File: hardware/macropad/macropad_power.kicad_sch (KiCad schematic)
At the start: 33 parts, among them J1 Conn_01x04_Pin, J2 USB_C_Receptacle, J3 Conn_02x03_Counter_Clockwise, J4 display(4x1), J5 enc1, J6 enc2, Q1 PMOS, SW1 SW_SPDT, SW10 SW_Push, SW11 SW_Push, SW2 SW_Push, SW3 SW_Push, SW4 SW_Push, SW5 SW_Push, SW6 SW_Push, SW7 SW_Push, SW8 SW_Push, SW9 SW_Push, U1 AP2112K-3.3, U2 STM32F103C8Tx, U3 NRF24L01_Breakout

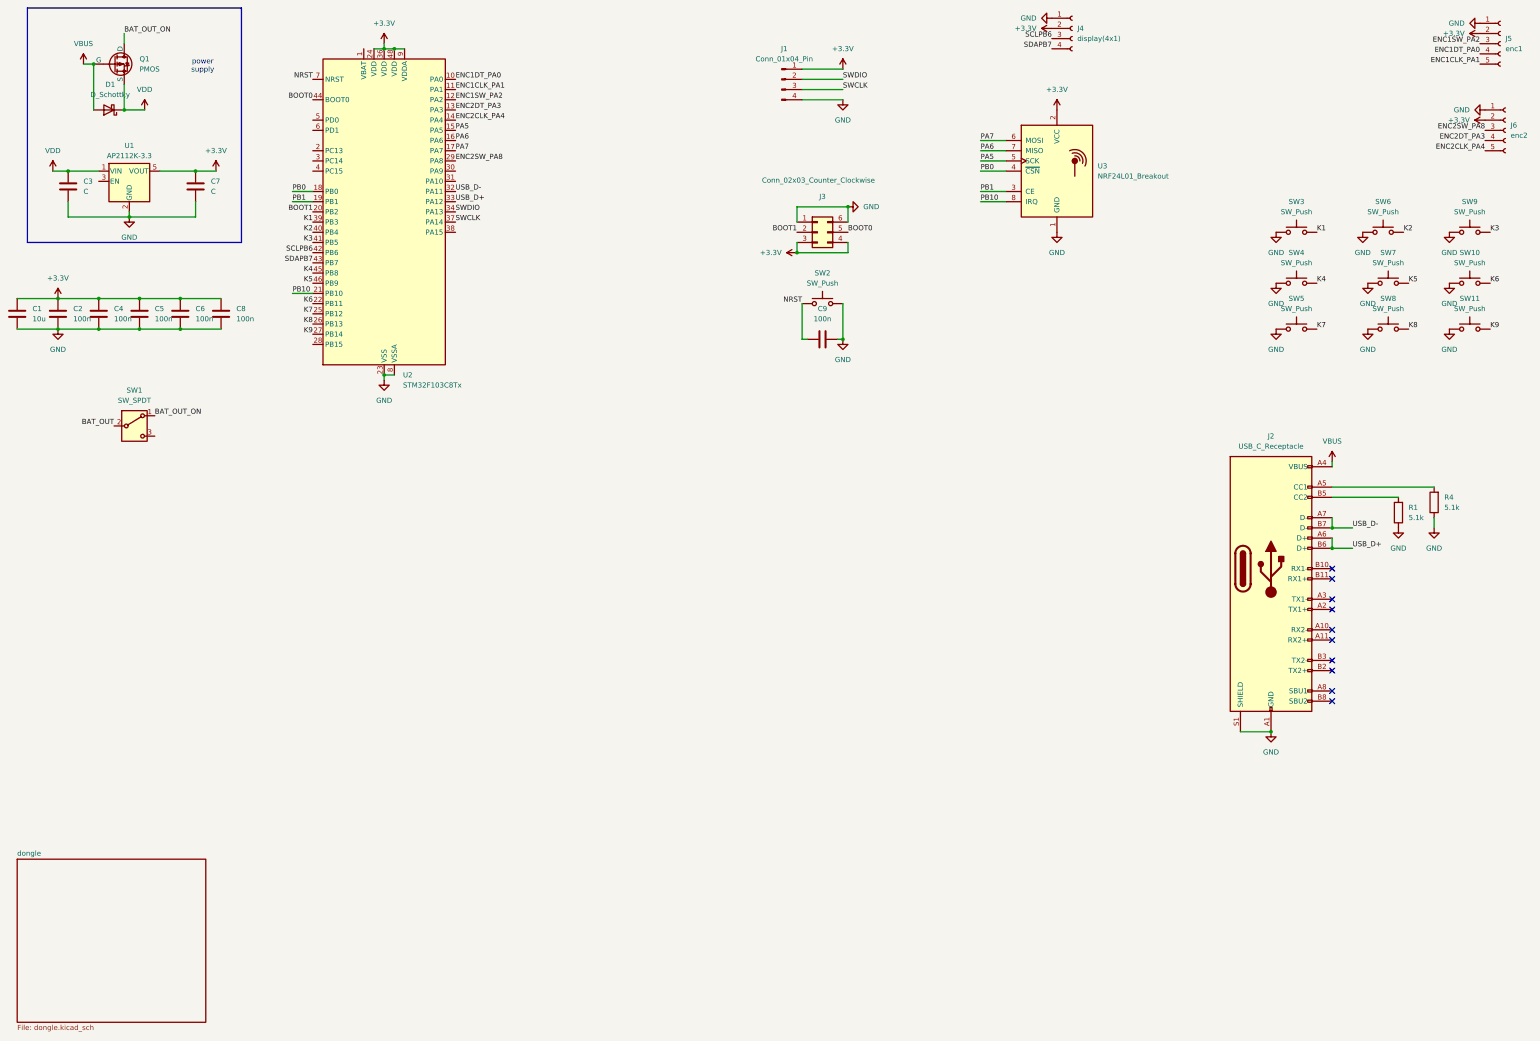
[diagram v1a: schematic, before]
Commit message: captured TP4056 module
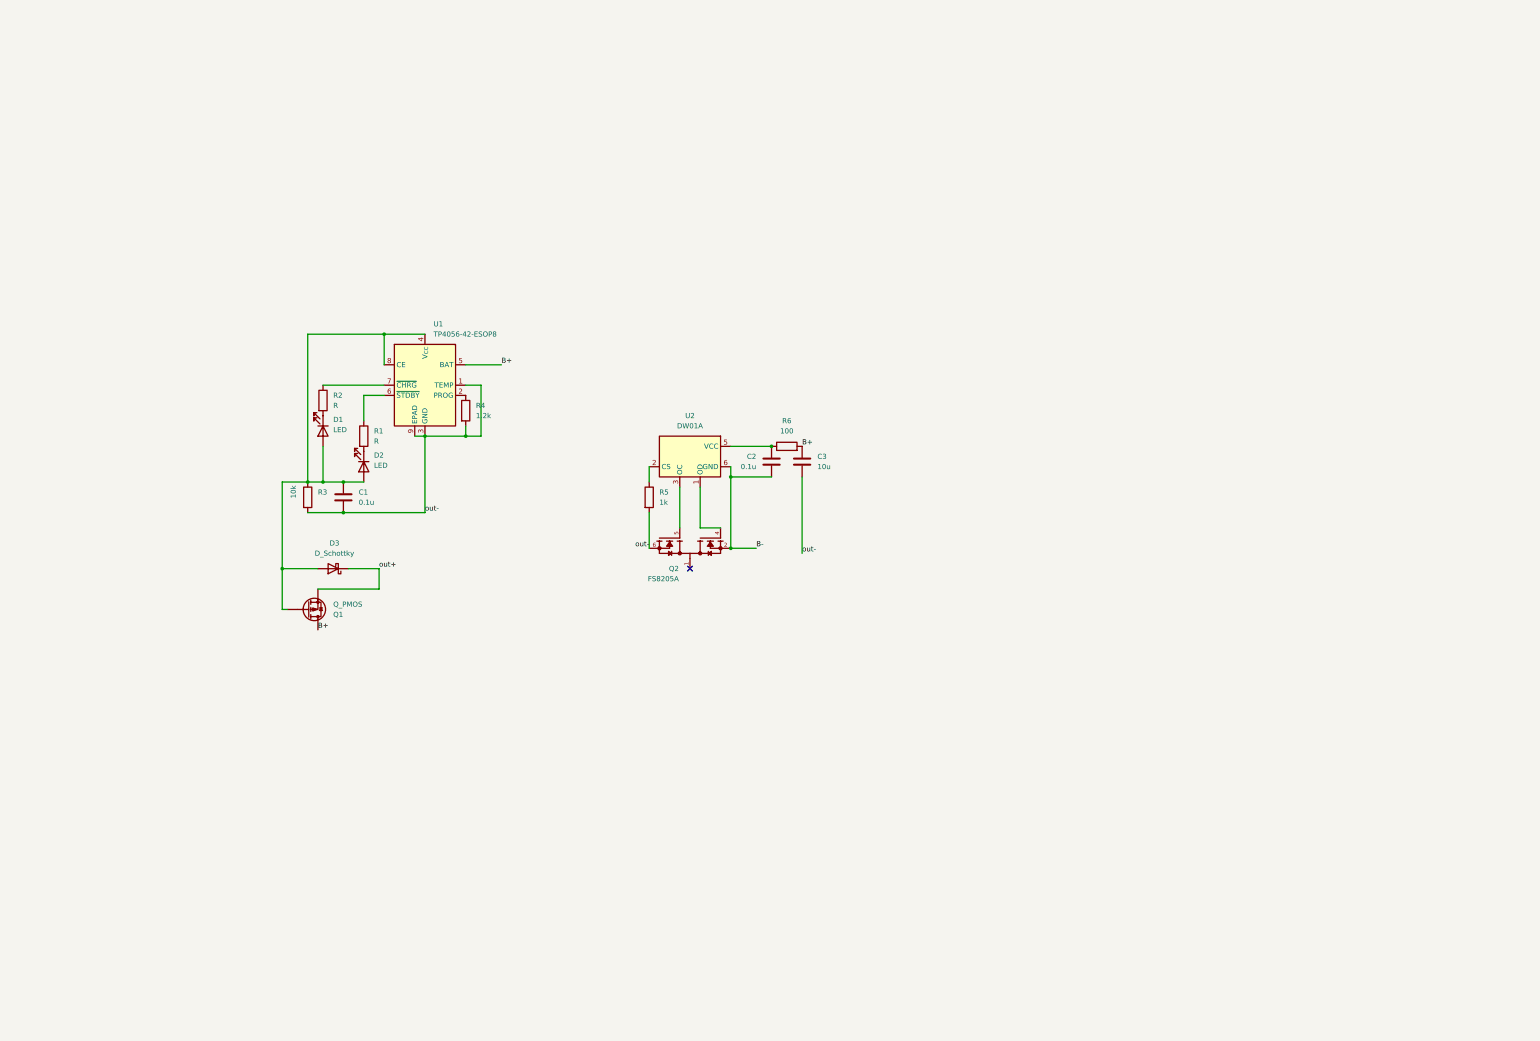
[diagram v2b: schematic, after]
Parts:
- removed C4, C5, C6, C8, C9: 100n, symbol Device:C
- removed C7: C, symbol Device:C
- removed D1: D_Schottky, symbol Device:D_Schottky
- removed J1: Conn_01x04_Pin, Connector_PinHeader_2.54mm:PinHeader_1x04_P2.54mm_Horizontal, symbol Connector:Conn_01x04_Pin
- removed J2: USB_C_Receptacle, symbol Connector:USB_C_Receptacle
- removed J3: Conn_02x03_Counter_Clockwise, symbol Connector_Generic:Conn_02x03_Counter_Clockwise
- removed J4: display(4x1), Connector_PinHeader_2.54mm:PinHeader_1x04_P2.54mm_Vertical, symbol Connector:Conn_01x04_Socket
- removed J5: enc1, Connector_PinHeader_2.54mm:PinHeader_1x05_P2.54mm_Horizontal, symbol Connector:Conn_01x05_Socket
- removed J6: enc2, Connector_PinHeader_2.54mm:PinHeader_1x05_P2.54mm_Horizontal, symbol Connector:Conn_01x05_Socket
- removed Q1: PMOS, symbol Simulation_SPICE:PMOS
- removed SW1: SW_SPDT, symbol Switch:SW_SPDT
- removed SW10, SW11, SW3, SW4, SW5, SW6, SW7, SW8, SW9: SW_Push, keyswitches:Kailh_socket_MX, symbol Switch:SW_Push
- removed SW2: SW_Push, symbol Switch:SW_Push
- removed U1: AP2112K-3.3, Package_TO_SOT_SMD:SOT-23-5, symbol Regulator_Linear:AP2112K-3.3
- removed U2: STM32F103C8Tx, Package_QFP:LQFP-48_7x7mm_P0.5mm, symbol MCU_ST_STM32F1:STM32F103C8Tx
- removed U3: NRF24L01_Breakout, RF_Module:nRF24L01_Breakout, symbol RF:NRF24L01_Breakout
- added D1, D2: LED, symbol Device:LED
- added D3: D_Schottky, symbol Device:D_Schottky
- added Q1: Q_PMOS, symbol Device:Q_PMOS
- added Q2: FS8205A, FS8205A:SOP65P640X120-8N, symbol FS8205A:FS8205A
- added R2: R, symbol Device:R
- added R3: 10k, symbol Device:R
- added R5: 1k, symbol Device:R
- added R6: 100, symbol Device:R
- added U1: TP4056-42-ESOP8, Package_SO:SOIC-8-1EP_3.9x4.9mm_P1.27mm_EP2.41x3.3mm_ThermalVias, symbol Battery_Management:TP4056-42-ESOP8
- added U2: DW01A, Package_TO_SOT_SMD:SOT-23-6, symbol Battery_Management:DW01A
- C1: value 10u -> 0.1u
- C2: value 100n -> 0.1u
- C3: value C -> 10u
- R1: value 5.1k -> R
- R4: value 5.1k -> 1.2k
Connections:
- net out-: now reaches R4.2
- net out-: now also C1.2, C3.2, Q2.6, Q2.7, R3.2, R5.2, U1.1 (TEMP), U1.3 (GND), U1.9 (EPAD)
- net at R1.2: now also D2.1 (K)
- net +3.3V: no longer names the net of C1.1
- net +3.3V: now also D1.2 (A), D2.2 (A), D3.2 (A), Q1.G, R3.1, U1.4 (V_{CC}), U1.8 (CE); no longer C2.1
- removed net GND: C1.2, C2.2, C3.2, R1.1, R4.1
- net VDD renamed B+
- net B+: now also Q1.D, R6.2, U1.5 (BAT)
- new net: R1.1, U1.6 (~{STDBY})
- new net: D1.1 (K), R2.2
- new net: R5.1, U2.2 (CS)
- new net: R4.1, U1.2 (PROG)
- new net: C2.1, R6.1, U2.5 (VCC)
- new net: R2.1, U1.7 (~{CHRG})
- new net: Q2.1, Q2.8
- new net: Q2.4, U2.1 (OD)
- new net: Q2.5, U2.3 (OC)
- new net B-: C2.2, Q2.2, Q2.3, U2.6 (GND)
- new net out+: D3.1 (K), Q1.S
- no-connect marks 10 -> 1
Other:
- removed sheet dongle
- note removed: "power supply"

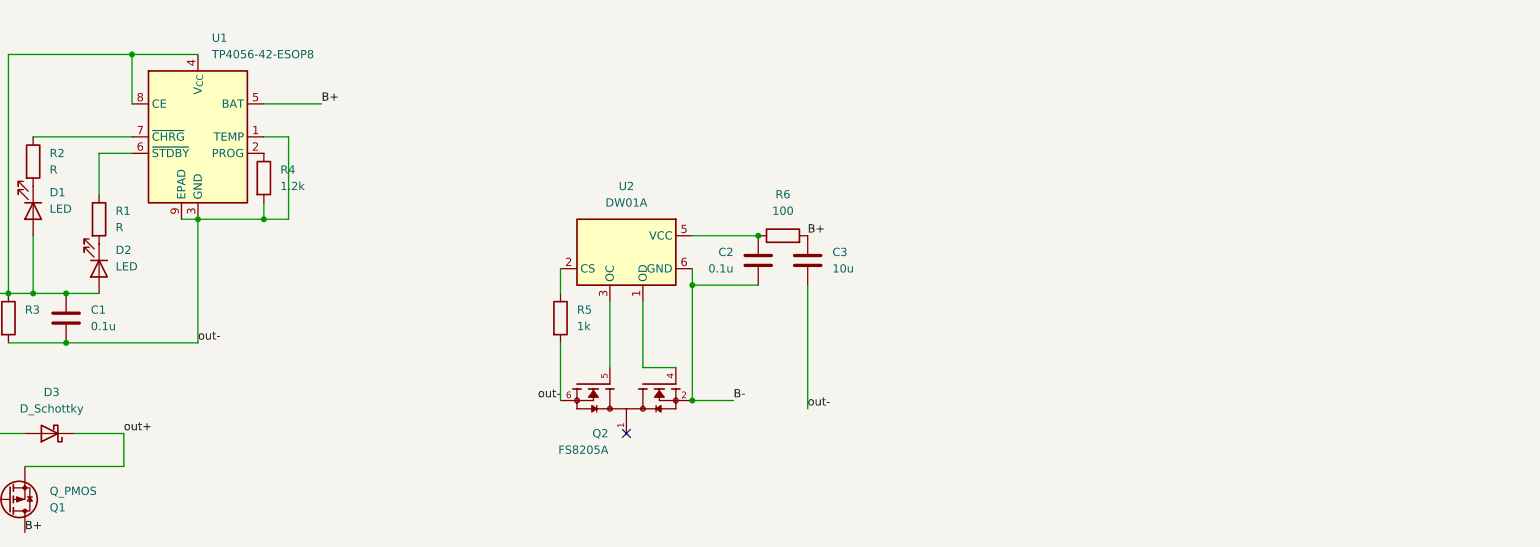
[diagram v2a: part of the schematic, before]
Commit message: captured the Buck(3_3V)
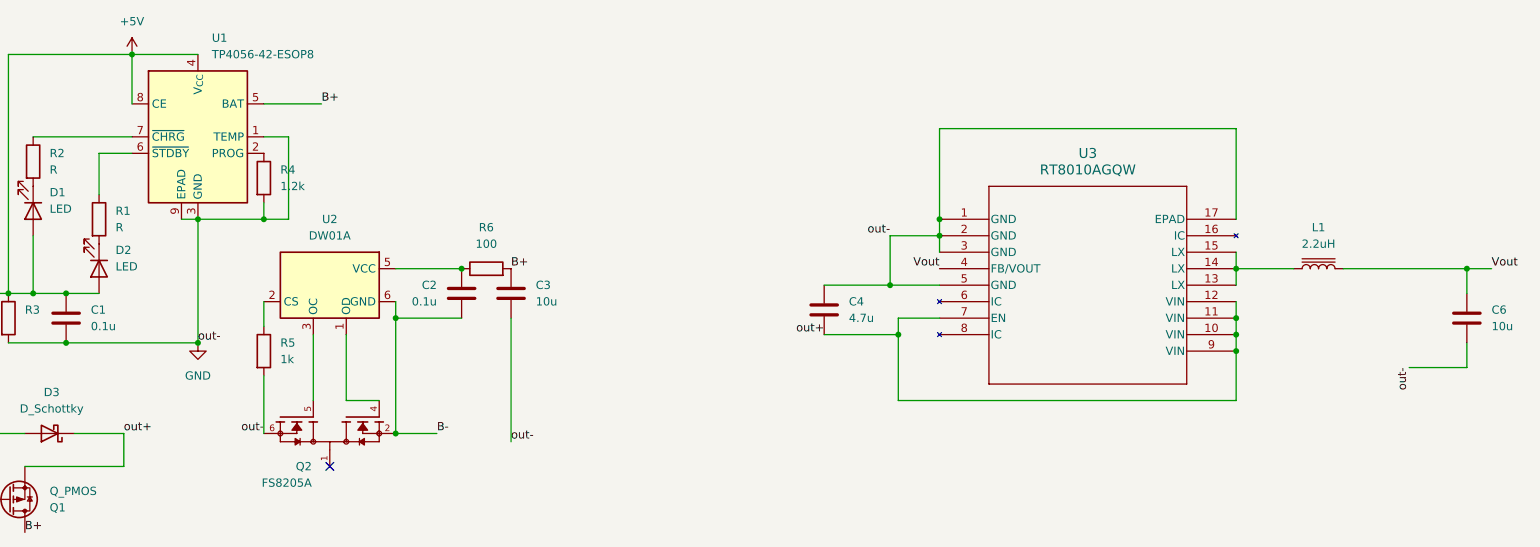
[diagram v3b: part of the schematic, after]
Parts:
- added C4: 4.7u, symbol Device:C
- added C6: 10u, symbol Device:C
- added L1: 2.2uH, symbol Device:L_Iron
- added U3: RT8010AGQW, WQFN16_RT8010_RIT, symbol 2026-02-28_18-02-32:RT8010AGQW
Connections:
- net out+: now also C4.2, U3.10 (VIN), U3.11 (VIN), U3.12 (VIN), U3.7 (EN), U3.9 (VIN)
- net +5V: now reaches C1.1, D1.2 (A), D2.2 (A), D3.2 (A), Q1.G, R3.1, U1.4 (V_{CC}), U1.8 (CE)
- net out- renamed GND
- net GND: now also C4.1, C6.2, U3.1 (GND), U3.17 (EPAD), U3.2 (GND), U3.3 (GND), U3.5 (GND)
- new net: L1.1, U3.13 (LX), U3.14 (LX), U3.15 (LX)
- new net Vout: C6.1, L1.2, U3.4 (FB/VOUT)
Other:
- moved on the sheet: C2, C3, Q2, R5, R6, U2

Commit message: added 1k resistors to leds
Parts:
- R1, R2: value R -> 1k
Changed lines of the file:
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@@
 		(dnp no)
 		(fields_autoplaced yes)
-		(property "Reference" "R?"
+		(property "Reference" "R1"
 			(at 113.03 120.6499 0)
 			(effects
@@
 			)
 		)
-		(property "Value" "R"
+		(property "Value" "1k"
 			(at 113.03 123.1899 0)
 			(effects
@@
 					(unit 1)
 				)
-				(path "/228dc472-b306-4e5f-8dc5-2bf23eb4978d/5b38d27c-d7f4-4a8d-8a5e-966bba03fead"
-					(reference "R?")
-					(unit 1)
-				)
 			)
 		)
@@
 		(dnp no)
 		(fields_autoplaced yes)
-		(property "Reference" "#PWR?"
+		(property "Reference" "#PWR02"
 			(at 125.73 147.32 0)
 			(effects
@@
 					(unit 1)
 				)
-				(path "/228dc472-b306-4e5f-8dc5-2bf23eb4978d/5b38d27c-d7f4-4a8d-8a5e-966bba03fead"
-					(reference "#PWR?")
-					(unit 1)
-				)
 			)
 		)
@@
 		(dnp no)
 		(fields_autoplaced yes)
-		(property "Reference" "D?"
+		(property "Reference" "D1"
 			(at 102.87 117.7924 90)
 			(effects
@@
 					(unit 1)
 				)
-				(path "/228dc472-b306-4e5f-8dc5-2bf23eb4978d/5b38d27c-d7f4-4a8d-8a5e-966bba03fead"
-					(reference "D?")
-					(unit 1)
-				)
 			)
 		)
@@
 		(dnp no)
 		(fields_autoplaced yes)
-		(property "Reference" "R?"
+		(property "Reference" "R5"
 			(at 138.43 140.9699 0)
 			(effects
@@
 					(unit 1)
 				)
-				(path "/228dc472-b306-4e5f-8dc5-2bf23eb4978d/5b38d27c-d7f4-4a8d-8a5e-966bba03fead"
-					(reference "R?")
-					(unit 1)
-				)
 			)
 		)
@@
 		(dnp no)
 		(fields_autoplaced yes)
-		(property "Reference" "L?"
+		(property "Reference" "L1"
 			(at 298.45 123.19 90)
 			(effects
@@
 					(unit 1)
 				)
-				(path "/228dc472-b306-4e5f-8dc5-2bf23eb4978d/5b38d27c-d7f4-4a8d-8a5e-966bba03fead"
-					(reference "L?")
-					(unit 1)
-				)
 			)
 		)
@@
 		(dnp no)
 		(fields_autoplaced yes)
-		(property "Reference" "R?"
+		(property "Reference" "R4"
 			(at 138.43 114.2999 0)
 			(effects
@@
 				(path "/228dc472-b306-4e5f-8dc5-2bf23eb4978d"
 					(reference "R4")
-					(unit 1)
-				)
-				(path "/228dc472-b306-4e5f-8dc5-2bf23eb4978d/5b38d27c-d7f4-4a8d-8a5e-966bba03fead"
-					(reference "R?")
 					(unit 1)
 				)
@@
 		(on_board yes)
 		(dnp no)
-		(property "Reference" "Q?"
+		(property "Reference" "Q1"
 			(at 102.87 166.3701 0)
 			(effects
@@
 					(unit 1)
 				)
-				(path "/228dc472-b306-4e5f-8dc5-2bf23eb4978d/5b38d27c-d7f4-4a8d-8a5e-966bba03fead"
-					(reference "Q?")
-					(unit 1)
-				)
 			)
 		)
@@
 		(dnp no)
 		(fields_autoplaced yes)
-		(property "Reference" "R?"
+		(property "Reference" "R6"
 			(at 170.18 123.19 90)
 			(effects
@@
 					(unit 1)
 				)
-				(path "/228dc472-b306-4e5f-8dc5-2bf23eb4978d/5b38d27c-d7f4-4a8d-8a5e-966bba03fead"
-					(reference "R?")
-					(unit 1)
-				)
 			)
 		)
@@
 		(on_board yes)
 		(dnp no)
-		(property "Reference" "R?"
+		(property "Reference" "R3"
 			(at 99.06 135.8899 0)
 			(effects
@@
 					(unit 1)
 				)
-				(path "/228dc472-b306-4e5f-8dc5-2bf23eb4978d/5b38d27c-d7f4-4a8d-8a5e-966bba03fead"
-					(reference "R?")
-					(unit 1)
-				)
 			)
 		)
@@
 		(dnp no)
 		(fields_autoplaced yes)
-		(property "Reference" "D?"
+		(property "Reference" "D2"
 			(at 113.03 126.6824 90)
 			(effects
@@
 					(unit 1)
 				)
-				(path "/228dc472-b306-4e5f-8dc5-2bf23eb4978d/5b38d27c-d7f4-4a8d-8a5e-966bba03fead"
-					(reference "D?")
-					(unit 1)
-				)
 			)
 		)
@@
 		(dnp no)
 		(fields_autoplaced yes)
-		(property "Reference" "D?"
+		(property "Reference" "D3"
 			(at 103.1875 148.59 0)
 			(effects
@@
 					(unit 1)
 				)
-				(path "/228dc472-b306-4e5f-8dc5-2bf23eb4978d/5b38d27c-d7f4-4a8d-8a5e-966bba03fead"
-					(reference "D?")
-					(unit 1)
-				)
 			)
 		)
@@
 		(dnp no)
 		(fields_autoplaced yes)
-		(property "Reference" "R?"
+		(property "Reference" "R2"
 			(at 102.87 111.7599 0)
 			(effects
@@
 			)
 		)
-		(property "Value" "R"
+		(property "Value" "1k"
 			(at 102.87 114.2999 0)
 			(effects
@@
 				(path "/228dc472-b306-4e5f-8dc5-2bf23eb4978d"
 					(reference "R2")
-					(unit 1)
-				)
-				(path "/228dc472-b306-4e5f-8dc5-2bf23eb4978d/5b38d27c-d7f4-4a8d-8a5e-966bba03fead"
-					(reference "R?")
 					(unit 1)
 				)
@@
 		(dnp no)
 		(fields_autoplaced yes)
-		(property "Reference" "C?"
+		(property "Reference" "C2"
 			(at 162.56 132.0799 0)
 			(effects
@@
 				(path "/228dc472-b306-4e5f-8dc5-2bf23eb4978d"
 					(reference "C2")
-					(unit 1)
-				)
-				(path "/228dc472-b306-4e5f-8dc5-2bf23eb4978d/5b38d27c-d7f4-4a8d-8a5e-966bba03fead"
-					(reference "C?")
 					(unit 1)
 				)
@@
 		(on_board yes)
 		(dnp no)
-		(property "Reference" "Q?"
+		(property "Reference" "Q2"
 			(at 143.2813 160.02 90)
 			(effects
@@
 					(unit 1)
 				)
-				(path "/228dc472-b306-4e5f-8dc5-2bf23eb4978d/5b38d27c-d7f4-4a8d-8a5e-966bba03fead"
-					(reference "Q?")
-					(unit 1)
-				)
 			)
 		)
@@
 		(dnp no)
 		(fields_autoplaced yes)
-		(property "Reference" "C?"
+		(property "Reference" "C3"
 			(at 177.8 132.0799 0)
 			(effects
@@
 					(unit 1)
 				)
-				(path "/228dc472-b306-4e5f-8dc5-2bf23eb4978d/5b38d27c-d7f4-4a8d-8a5e-966bba03fead"
-					(reference "C?")
-					(unit 1)
-				)
 			)
 		)
@@
 		(dnp no)
 		(fields_autoplaced yes)
-		(property "Reference" "#PWR?"
+		(property "Reference" "#PWR01"
 			(at 115.57 100.33 0)
 			(effects
@@
 				(path "/228dc472-b306-4e5f-8dc5-2bf23eb4978d"
 					(reference "#PWR01")
-					(unit 1)
-				)
-				(path "/228dc472-b306-4e5f-8dc5-2bf23eb4978d/5b38d27c-d7f4-4a8d-8a5e-966bba03fead"
-					(reference "#PWR?")
 					(unit 1)
 				)
@@
 		(dnp no)
 		(fields_autoplaced yes)
-		(property "Reference" "U?"
+		(property "Reference" "U2"
 			(at 146.05 121.92 0)
 			(effects
@@
 					(unit 1)
 				)
-				(path "/228dc472-b306-4e5f-8dc5-2bf23eb4978d/5b38d27c-d7f4-4a8d-8a5e-966bba03fead"
-					(reference "U?")
-					(unit 1)
-				)
 			)
 		)
@@
 		(dnp no)
 		(fields_autoplaced yes)
-		(property "Reference" "C?"
+		(property "Reference" "C4"
 			(at 226.06 134.6199 0)
 			(effects
@@
 					(unit 1)
 				)
-				(path "/228dc472-b306-4e5f-8dc5-2bf23eb4978d/5b38d27c-d7f4-4a8d-8a5e-966bba03fead"
-					(reference "C?")
-					(unit 1)
-				)
 			)
 		)
@@
 		(dnp no)
 		(fields_autoplaced yes)
-		(property "Reference" "U?"
+		(property "Reference" "U3"
 			(at 262.89 111.76 0)
 			(effects
@@
 					(unit 1)
 				)
-				(path "/228dc472-b306-4e5f-8dc5-2bf23eb4978d/5b38d27c-d7f4-4a8d-8a5e-966bba03fead"
-					(reference "U?")
-					(unit 1)
-				)
 			)
 		)
@@
 		(dnp no)
 		(fields_autoplaced yes)
-		(property "Reference" "U?"
+		(property "Reference" "U1"
 			(at 127.8733 93.98 0)
 			(effects
@@
 					(unit 1)
 				)
-				(path "/228dc472-b306-4e5f-8dc5-2bf23eb4978d/5b38d27c-d7f4-4a8d-8a5e-966bba03fead"
-					(reference "U?")
-					(unit 1)
-				)
 			)
 		)
@@
 		(dnp no)
 		(fields_autoplaced yes)
-		(property "Reference" "C?"
+		(property "Reference" "C1"
 			(at 109.22 135.8899 0)
 			(effects
@@
 					(unit 1)
 				)
-				(path "/228dc472-b306-4e5f-8dc5-2bf23eb4978d/5b38d27c-d7f4-4a8d-8a5e-966bba03fead"
-					(reference "C?")
-					(unit 1)
-				)
 			)
 		)
@@
 		(dnp no)
 		(fields_autoplaced yes)
-		(property "Reference" "C?"
+		(property "Reference" "C6"
 			(at 325.12 135.8899 0)
 			(effects
@@
 					(unit 1)
 				)
-				(path "/228dc472-b306-4e5f-8dc5-2bf23eb4978d/5b38d27c-d7f4-4a8d-8a5e-966bba03fead"
-					(reference "C?")
-					(unit 1)
-				)
